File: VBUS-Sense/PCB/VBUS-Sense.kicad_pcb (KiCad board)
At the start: 2 copper layers, 25 x 45 mm, 25 parts, among them J1 Conn_01x01, J2 Conn_01x01, J3 Conn_01x04, T1 TRANS-2CT, U1 AMC1301, U2 SN6501DBV, U3 TPS76350

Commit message: Vsense
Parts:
- R27, R29: footprint Resistors_SMD:R_0805_HandSoldering -> Resistors_SMD:R_1206
- moved C37 3.09 mm to (7.09, 28.6)
- moved C9 3.09 mm to (4.98, 26.6)
- moved D9 3.09 mm to (5.11, 32.6)
- moved R28 3.09 mm to (2.39, 28.7)
- moved R27 1.12 mm to (14.0, 35.5)
- moved U2 0.51 mm to (20.1, 7.67)
- moved C39 0.28 mm to (3.89, 5.00)
- moved C40 0.28 mm to (3.89, 6.88)
- moved C4 0.10 mm to (19.9, 26.7)
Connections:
- U3 pad 4: Net-(U3-Pad4) -> (no net)
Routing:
- net +5V: track 0.00 -> 15.5 mm, vias 0 -> 4
- net /V_PHASE/VBUS-: track 0.00 -> 14.8 mm, vias 0 -> 3
- net Net-(C38-Pad1): track 0.00 -> 14.1 mm
- net Net-(C37-Pad1): track 0.00 -> 13.8 mm
- net Net-(C3-Pad1): track 0.00 -> 13.3 mm
- net /V_PHASE/Vout-: track 0.00 -> 10.3 mm
- net /V_PHASE/Vout+: track 0.00 -> 9.75 mm
- net Net-(C38-Pad2): track 0.00 -> 9.38 mm
- net /V_PHASE/VBUS+: track 0.00 -> 7.29 mm
- net GND: track 0.00 -> 6.99 mm, vias 0 -> 2
- net /V_PHASE/+VCC: track 0.00 -> 4.90 mm, vias 0 -> 2
- net Net-(D2-Pad2): track 0.00 -> 2.88 mm
- net Net-(D1-Pad2): track 0.00 -> 2.84 mm
- net Net-(T1-Pad3): track 0.00 -> 2.78 mm
- net Net-(T1-Pad1): track 0.00 -> 2.75 mm
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- added copper zone on B.Cu, net +5V
- added copper zone on B.Cu, net /V_PHASE/+VCC
- added copper zone on F.Cu, net /V_PHASE/VBUS-
- added copper zone on F.Cu, net GND

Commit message: V0.2 PCB
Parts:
- removed C2, C4: 100n, Capacitors_SMD:C_0805_HandSoldering
- removed C3, C5: 22u, Capacitors_SMD:C_0805_HandSoldering
- removed D1, D2: MBR0520, Diodes_SMD:D_SOD-123
- removed T1: TRANS-2CT, ENNOID:WURTH-760390014
- removed U3: TPS76350, TO_SOT_Packages_SMD:SOT-23-5_HandSoldering
- added C10: 100n, Capacitors_SMD:C_0805_HandSoldering, F.Cu at (75.1, 18.6)
- added C11: 1u, Capacitors_SMD:C_0805_HandSoldering, F.Cu at (75.1, 24.1)
- added C12: 1u, Capacitors_SMD:C_0805_HandSoldering, F.Cu at (80.0, 18.6)
- added FL2: ACM4520, ENNOID:ACM4520, F.Cu at (21.4, 5.05)
- added Q1: Q_NMOS_GDS, TO_SOT_Packages_SMD:TO-252-2, F.Cu at (30.6, 24.1)
- added R1: 20k, Resistors_SMD:R_2512_HandSoldering, F.Cu at (20.1, 34.6)
- added R2: 20k, Resistors_SMD:R_2512_HandSoldering, B.Cu at (20.1, 34.5)
- added R3: 20k, Resistors_SMD:R_2512_HandSoldering, F.Cu at (33.1, 34.4)
- added R4: 20k, Resistors_SMD:R_2512_HandSoldering, B.Cu at (33.0, 34.4)
- C1: value 2.2u -> 1u
- U2: value SN6501DBV -> NMV; footprint TO_SOT_Packages_SMD:SOT-23-5_HandSoldering -> ENNOID:DCDC-Conv_muRata_MGJ2
- moved U2 4.03 mm to (22.0, 11.2), turned to 0 degrees
- moved U1 1.63 mm to (3.63, 15.9)
- moved R27 0.77 mm to (13.2, 35.3)
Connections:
- C1 pad 1: +5V -> /ISO_PSU/COM
- C1 pad 2: GND -> /ISO_PSU/-VEE
- C37 pad 2: /V_PHASE/VBUS- -> /ISO_PSU/COM
- C9 pad 2: /V_PHASE/VBUS- -> /ISO_PSU/COM
- D9 pad 2: /V_PHASE/VBUS- -> /ISO_PSU/COM
- J2 pad 1: /V_PHASE/VBUS- -> /ISO_PSU/COM
- R28 pad 2: /V_PHASE/+VCC -> /ISO_PSU/+VCC
- R30 pad 1: /V_PHASE/VBUS- -> /ISO_PSU/COM
- R31 pad 1: /V_PHASE/VBUS- -> /ISO_PSU/COM
- U1 pad 4: /V_PHASE/VBUS- -> /ISO_PSU/COM
- U2 pad 2: +5V -> Net-(C10-Pad2)
- U2 pad 5: GND -> /ISO_PSU/-VEE
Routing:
- net +5V: track 15.5 -> 0.00 mm, vias 4 -> 0
- net /V_PHASE/VBUS-: track 14.8 -> 0.00 mm, vias 3 -> 0
- net Net-(C38-Pad1): track 14.1 -> 0.00 mm
- net Net-(C37-Pad1): track 13.8 -> 0.00 mm
- net Net-(C3-Pad1): track 13.3 -> 0.00 mm
- net /V_PHASE/Vout-: track 10.3 -> 0.00 mm
- net /V_PHASE/Vout+: track 9.75 -> 0.00 mm
- net Net-(C38-Pad2): track 9.38 -> 0.00 mm
- net /V_PHASE/VBUS+: track 7.29 -> 0.00 mm
- net GND: track 6.99 -> 0.00 mm, vias 2 -> 0
- net /V_PHASE/+VCC: track 4.90 -> 0.00 mm, vias 2 -> 0
- net Net-(D2-Pad2): track 2.88 -> 0.00 mm
- net Net-(D1-Pad2): track 2.84 -> 0.00 mm
- net Net-(C10-Pad1): track 2.78 -> 0.00 mm
- net Net-(T1-Pad1): track 2.75 -> 0.00 mm
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
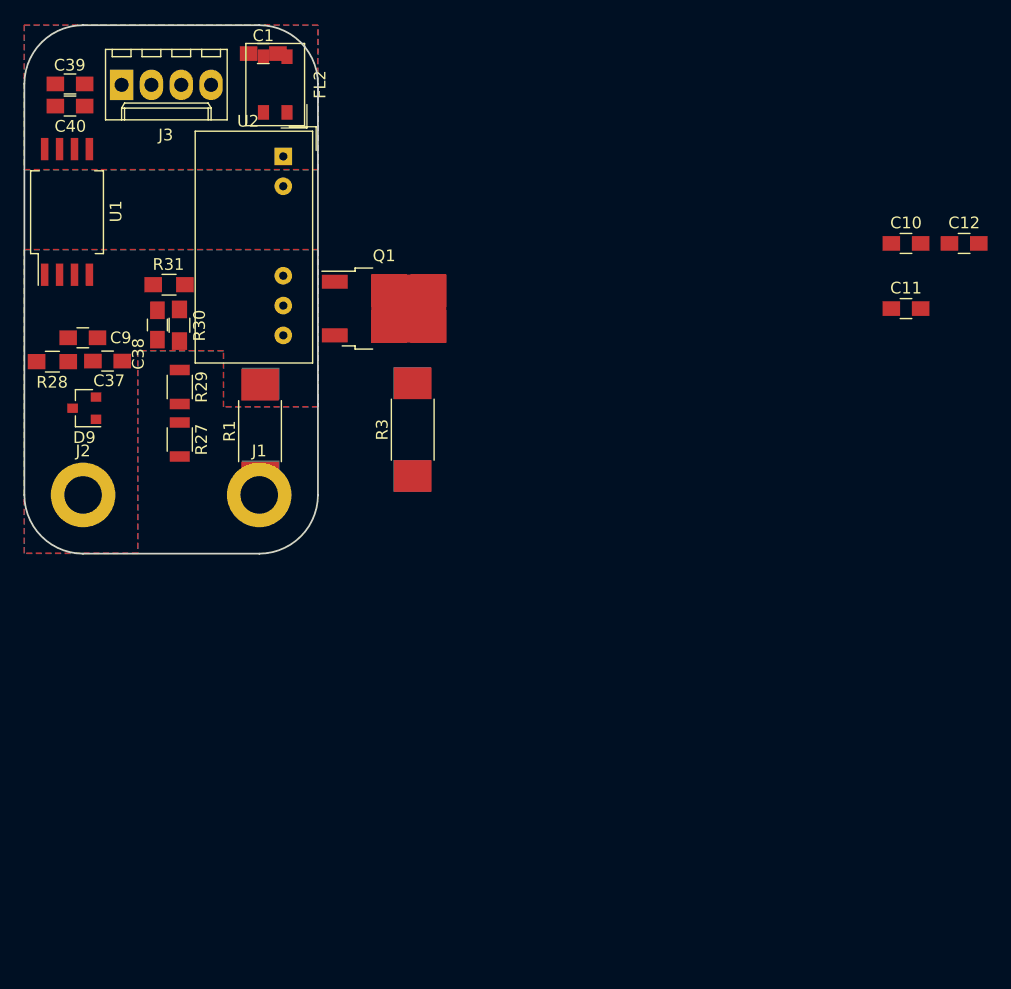
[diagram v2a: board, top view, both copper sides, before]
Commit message: VBUS update
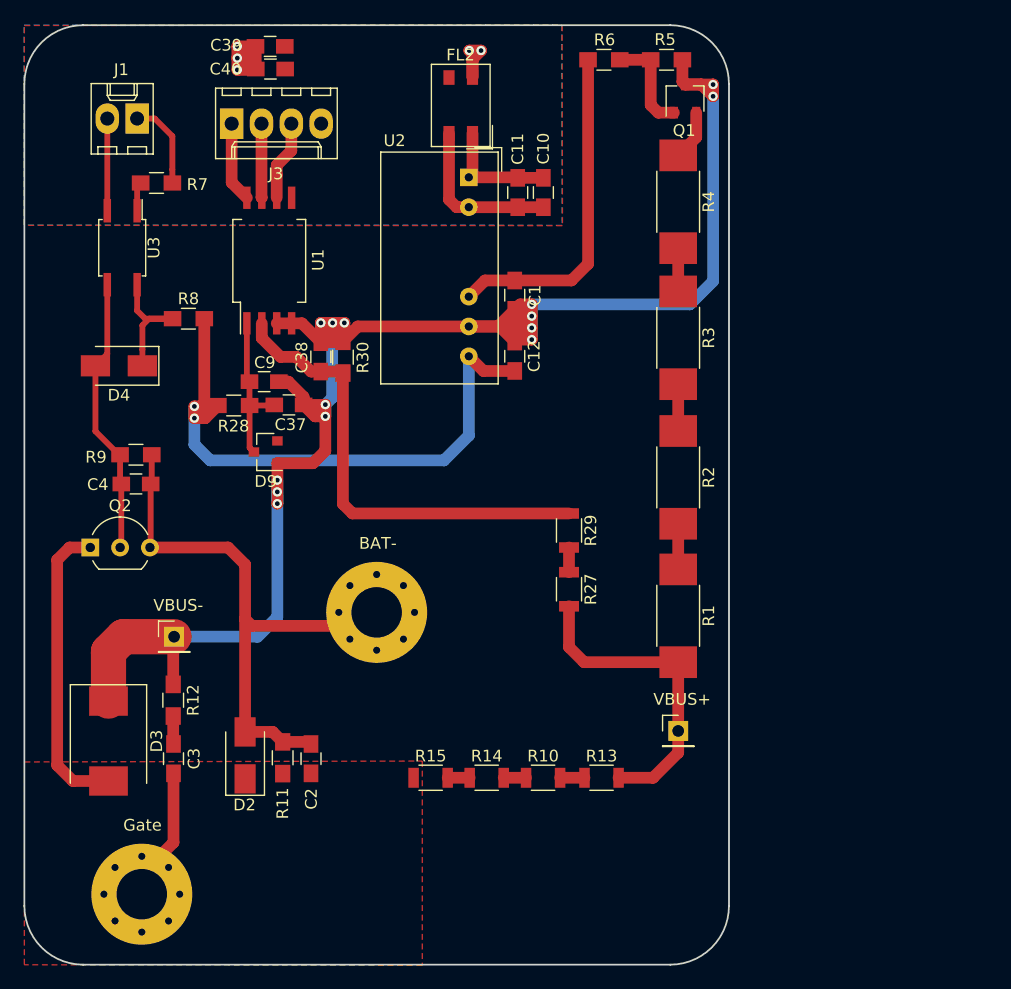
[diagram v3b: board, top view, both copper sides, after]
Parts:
- removed J2: Conn_01x01, Mounting_Holes:MountingHole_3.2mm_M3_ISO14580_Pad
- removed R31: 1k, Resistors_SMD:R_0805_HandSoldering
- added C2: 0.15u, Capacitors_SMD:C_0805_HandSoldering, F.Cu at (24.4, 62.5)
- added C3: 0.15u, Capacitors_SMD:C_0805_HandSoldering, F.Cu at (12.7, 62.5)
- added C4: DNP, Capacitors_SMD:C_0805_HandSoldering, F.Cu at (9.51, 39.1)
- added D2: D_Zener 18V SMAJ18CA, Diodes_SMD:D_SMA, F.Cu at (18.8, 62.2)
- added D3: D_Zener 440v SMJC440CA, Diodes_SMD:D_SMC, F.Cu at (7.16, 61.0)
- added D4: D_Zener 12V, Diodes_SMD:D_SMA, F.Cu at (8.05, 29.0)
- added MK1: VBUS-, Pin_Headers:Pin_Header_Straight_1x01_Pitch2.54mm, F.Cu at (12.8, 52.1)
- added MK2: VBUS+, Pin_Headers:Pin_Header_Straight_1x01_Pitch2.54mm, F.Cu at (55.7, 60.1)
- added MK3: Gate, Mounting_Holes:MountingHole_4.3mm_M4_Pad_Via, F.Cu at (10.0, 74.0)
- added MK4: BAT-, Mounting_Holes:MountingHole_4.3mm_M4_Pad_Via, F.Cu at (30.0, 50.0)
- added Q2: BC546, TO_SOT_Packages_THT:TO-92_Inline_Wide, F.Cu at (5.61, 44.5)
- added R10: 200k, Resistors_SMD:R_1206, F.Cu at (44.2, 64.1)
- added R11: 30k, Resistors_SMD:R_0805_HandSoldering, F.Cu at (22.0, 62.4)
- added R12: 1k, Resistors_SMD:R_0805_HandSoldering, F.Cu at (12.7, 57.5)
- added R13: 200k, Resistors_SMD:R_1206, F.Cu at (49.1, 64.1)
- added R14: 200k, Resistors_SMD:R_1206, F.Cu at (39.4, 64.1)
- added R15: 200k, Resistors_SMD:R_1206, F.Cu at (34.6, 64.1)
- added R5: 20k, Resistors_SMD:R_0805_HandSoldering, F.Cu at (54.7, 2.95)
- added R6: 100, Resistors_SMD:R_0805_HandSoldering, F.Cu at (49.4, 2.95)
- added R7: 1k, Resistors_SMD:R_0805_HandSoldering, F.Cu at (11.3, 13.4)
- added R8: 10k, Resistors_SMD:R_0805_HandSoldering, F.Cu at (14.0, 25.0)
- added R9: 10k, Resistors_SMD:R_0805_HandSoldering, F.Cu at (9.50, 36.6)
- added U3: LTV-356T, Housings_SOIC:SO-4_4.4x3.6mm_Pitch2.54mm, F.Cu at (8.33, 18.9)
- J1: value Conn_01x01 -> Conn_01x02 E-STOP; footprint Mounting_Holes:MountingHole_3.2mm_M3_ISO14580_Pad -> Connectors_Molex:Molex_KK-6410-02_02x2.54mm_Straight
- Q1: value Q_NMOS_GDS -> Depletion mode FET ex: CPC3982; footprint TO_SOT_Packages_SMD:TO-252-2 -> TO_SOT_Packages_SMD:SOT-23W
- R2, R4: moved to F.Cu
- moved C12 39.5 mm to (41.8, 28.2), turned to 90 degrees
- moved R1 38.9 mm to (55.7, 50.3), turned to 270 degrees
- moved R2 35.8 mm to (55.7, 38.5)
- moved R27 35.5 mm to (46.4, 48.0)
- moved R29 35.3 mm to (46.4, 43.0)
- moved C11 34.5 mm to (42.0, 14.2), turned to 270 degrees
- moved J1 33.7 mm to (9.60, 7.95), turned to 180 degrees
- moved Q1 31.3 mm to (56.3, 6.25), turned to 90 degrees
- moved C10 31.2 mm to (44.2, 14.2), turned to 270 degrees
- moved R4 29.8 mm to (55.7, 15.0)
- moved C1 29.7 mm to (41.8, 23.0), turned to 90 degrees
- moved R3 23.9 mm to (55.7, 26.6), turned to 270 degrees
- moved U1 17.7 mm to (20.9, 20.0)
- moved C40 17.4 mm to (21.0, 3.73)
- moved C39 17.3 mm to (20.9, 1.80)
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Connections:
- net /V_PHASE/Vout+ renamed /V_BUS/Vout+
- net /V_PHASE/Vout- renamed /V_BUS/Vout-
- C38 pad 2: Net-(C38-Pad2) -> /ISO_PSU/COM
- J1 pad 1: /V_PHASE/VBUS+ -> /Inrush_Limiter/ON/OFF
- Q1 pad 1: /ISO_PSU/-VEE -> Net-(Q1-Pad1)
- R1 pad 2: /V_PHASE/VBUS+ -> /Inrush_Limiter/+VBUS
- R27 pad 2: /V_PHASE/VBUS+ -> /Inrush_Limiter/+VBUS
- U1 pad 3: Net-(C38-Pad2) -> /ISO_PSU/COM
- U2 pad 7: (no net) -> /ISO_PSU/+VCC
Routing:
- net /ISO_PSU/COM: track 0.00 -> 161.5 mm, vias 0 -> 14
- net /ISO_PSU/+VCC: track 0.00 -> 53.3 mm, vias 0 -> 2
- net /Inrush_Limiter/VBAT-: track 0.00 -> 48.9 mm
- net Net-(C38-Pad1): track 0.00 -> 40.1 mm
- net /Inrush_Limiter/GATE: track 0.00 -> 37.1 mm
- net /ISO_PSU/-VEE: track 0.00 -> 28.7 mm
- net /Inrush_Limiter/+VBUS: track 0.00 -> 27.0 mm
- net +5V: track 0.00 -> 23.9 mm, vias 0 -> 5
- net Net-(C4-Pad1): track 0.00 -> 23.8 mm
- net Net-(C10-Pad2): track 0.00 -> 13.9 mm
- net Net-(C37-Pad1): track 0.00 -> 13.3 mm
- net Net-(D4-Pad1): track 0.00 -> 11.8 mm
- net Net-(C10-Pad1): track 0.00 -> 10.2 mm
- net Net-(Q1-Pad1): track 0.00 -> 8.73 mm
- net /Inrush_Limiter/GND: track 0.00 -> 7.85 mm
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- added copper zone on F.Cu, net /Inrush_Limiter/GATE
- removed copper zone on B.Cu, net /V_PHASE/+VCC
- removed copper zone on F.Cu, net /V_PHASE/VBUS-
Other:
- board size 25 x 45 mm -> 60 x 80 mm

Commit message: VBUS-SENSE changes
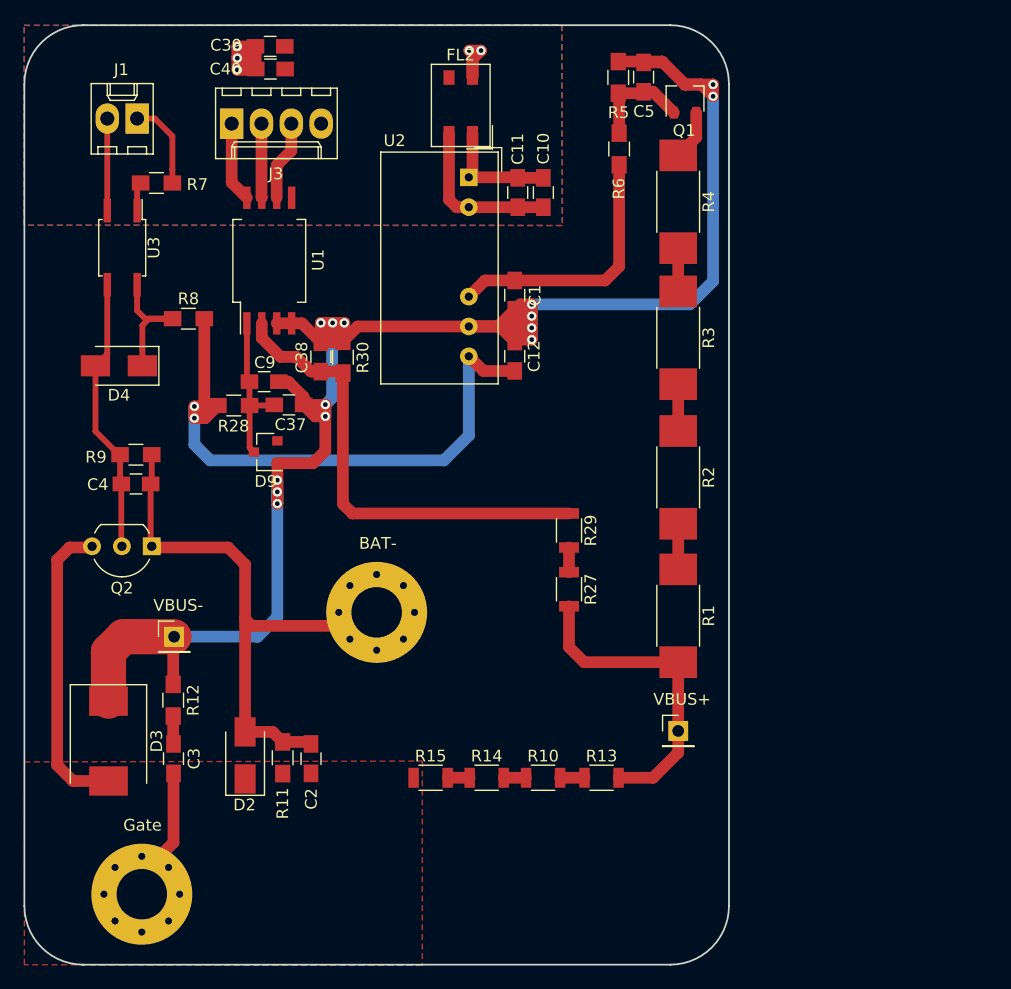
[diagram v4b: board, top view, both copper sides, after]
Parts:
- added C5: 100n, Capacitors_SMD:C_0805_HandSoldering, F.Cu at (52.7, 4.42)
- C4: value DNP -> 100n
- Q2: value BC546 -> 2N7000
- moved R6 7.70 mm to (50.6, 10.5), turned to 270 degrees
- moved Q2 5.23 mm to (10.8, 44.4), turned to 180 degrees
- moved R5 4.38 mm to (50.6, 4.45), turned to 270 degrees
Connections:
- Q2 pad 1: /Inrush_Limiter/GATE -> /Inrush_Limiter/VBAT-
- Q2 pad 3: /Inrush_Limiter/VBAT- -> /Inrush_Limiter/GATE
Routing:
- net /ISO_PSU/COM: track 161.5 -> 167.7 mm
- net /ISO_PSU/-VEE: track 28.7 -> 22.5 mm

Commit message: Maintenance update
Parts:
- removed D4: D_Zener 12V, Diodes_SMD:D_SMA
- added BZ1: Buzzer, Buzzers_Beepers:MagneticBuzzer_ProSignal_ABT-410-RC, F.Cu at (53.4, 19.6)
- added C7: 100n, Capacitors_SMD:C_0805_HandSoldering, F.Cu at (7.37, 11.1)
- added Q4: 2N7000, TO_SOT_Packages_THT:TO-92_Inline_Wide, F.Cu at (11.4, 44.4)
- added R16: 1k, Resistors_SMD:R_0805_HandSoldering, F.Cu at (13.0, 15.8)
- added R17: 1k, Resistors_SMD:R_0805_HandSoldering, F.Cu at (9.65, 29.6)
- added R18: 200k, Resistors_SMD:R_1206, F.Cu at (22.3, 51.8)
- C3: footprint Capacitors_SMD:C_0805_HandSoldering -> Capacitors_SMD:C_2225_HandSoldering
- J1: value Conn_01x02 E-STOP -> Conn_01x02 to external 12V power switch or VESC GPIO
- J3: value Conn_01x04 -> Conn_01x04 to vesc board
- MK4: value BAT- -> VBAT-
- R1, R2, R3, R4: value 20k -> 7.5K
- R7: value 1k -> 1M
- R8: value 10k -> 1k
- moved Q2 30.9 mm to (12.4, 13.5), turned to 90 degrees
- moved R8 20.5 mm to (11.0, 4.76), turned to 90 degrees
- moved MK2 14.0 mm to (55.9, 74.1)
- moved R1 14.0 mm to (55.9, 64.3)
- moved R2 14.0 mm to (55.9, 52.5)
- moved R3 14.0 mm to (55.9, 40.6)
- moved R4 14.0 mm to (55.9, 29.0)
- moved R12 7.40 mm to (18.7, 53.1)
- moved C2 4.19 mm to (28.6, 62.5)
- moved D2 4.19 mm to (23.0, 62.2)
- moved R11 4.19 mm to (26.2, 62.4)
- moved R7 3.97 mm to (7.30, 13.0)
- moved C3 3.68 mm to (16.1, 61.0)
- moved J1 3.66 mm to (6.60, 5.84)
- moved R6 2.34 mm to (51.0, 8.23), turned to 180 degrees
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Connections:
- J1 pad 2: /Inrush_Limiter/GND -> GND
- Q1 pad 2: Net-(Q1-Pad2) -> Net-(BZ1-Pad2)
- Q2 pad 1: /Inrush_Limiter/VBAT- -> Net-(Q2-Pad1)
- Q2 pad 2: Net-(C4-Pad1) -> Net-(C7-Pad1)
- Q2 pad 3: /Inrush_Limiter/GATE -> +5V
- R4 pad 1: Net-(Q1-Pad2) -> Net-(BZ1-Pad1)
- R7 pad 1: /Inrush_Limiter/ON/OFF -> Net-(C7-Pad1)
- R7 pad 2: Net-(R7-Pad2) -> GND
- R8 pad 1: Net-(D4-Pad1) -> Net-(C7-Pad1)
- R8 pad 2: /ISO_PSU/+VCC -> /Inrush_Limiter/ON/OFF
- U3 pad 1: Net-(R7-Pad2) -> Net-(R16-Pad1)
- U3 pad 2: /Inrush_Limiter/GND -> GND
- U3 pad 4: Net-(D4-Pad1) -> Net-(R17-Pad1)
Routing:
- net Net-(R2-Pad1): track 3.99 -> 113.0 mm, vias 0 -> 12
- net Net-(R3-Pad1): track 3.68 -> 90.0 mm, vias 0 -> 12
- net Net-(R1-Pad1): track 3.89 -> 87.0 mm, vias 0 -> 12
- net Net-(BZ1-Pad1): track 0.00 -> 65.9 mm, vias 0 -> 8
- net /Inrush_Limiter/+VBUS: track 27.0 -> 88.5 mm, vias 0 -> 8
- net /Inrush_Limiter/VBAT-: track 48.9 -> 78.6 mm, vias 0 -> 4
- net /Inrush_Limiter/GATE: track 37.1 -> 54.0 mm, vias 0 -> 3
- net /ISO_PSU/COM: track 167.7 -> 182.3 mm, vias 14 -> 19
- net /ISO_PSU/+VCC: track 53.3 -> 38.9 mm, vias 2 -> 3
- net Net-(D4-Pad1): track 11.8 -> 0.00 mm
- net Net-(C7-Pad1): track 0.00 -> 11.5 mm
- net Net-(BZ1-Pad2): track 0.00 -> 9.38 mm
- net /Inrush_Limiter/GND: track 7.85 -> 0.00 mm
- net Net-(R17-Pad1): track 0.00 -> 6.17 mm
- net +5V: track 23.9 -> 19.5 mm, vias 5 -> 2
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
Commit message: Maintenance update
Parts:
- added LOGO1: Logo_ENNOID, ENNOID:ENNOID-LOGO, B.Cu at (30.0, 62.5)
- C3: footprint Capacitors_SMD:C_2225_HandSoldering -> Capacitors_SMD:C_1812_HandSoldering
- U2: value NMV -> MGJ2
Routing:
- net /ISO_PSU/COM: track 182.3 -> 187.3 mm
- net /Inrush_Limiter/GATE: track 54.0 -> 56.0 mm
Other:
- board text added: "VBUS-Sense V0.1 01/2018 https://github.com/EnnoidMe"
